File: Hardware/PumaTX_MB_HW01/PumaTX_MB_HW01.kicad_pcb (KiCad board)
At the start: 4 copper layers, 130 x 40 mm, 121 parts, among them J100 FH12A-26S-0.5SH_55_, J101 FH12-12S-0.5SH_55_, J102 500334-0160, J103 500334-0160, J104 692122030100, J105 53398-0667, J400 U.FL-R-SMT-1_40_, J410 U.FL-R-SMT-1_40_, M130 Motor_DC, M140 Fan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

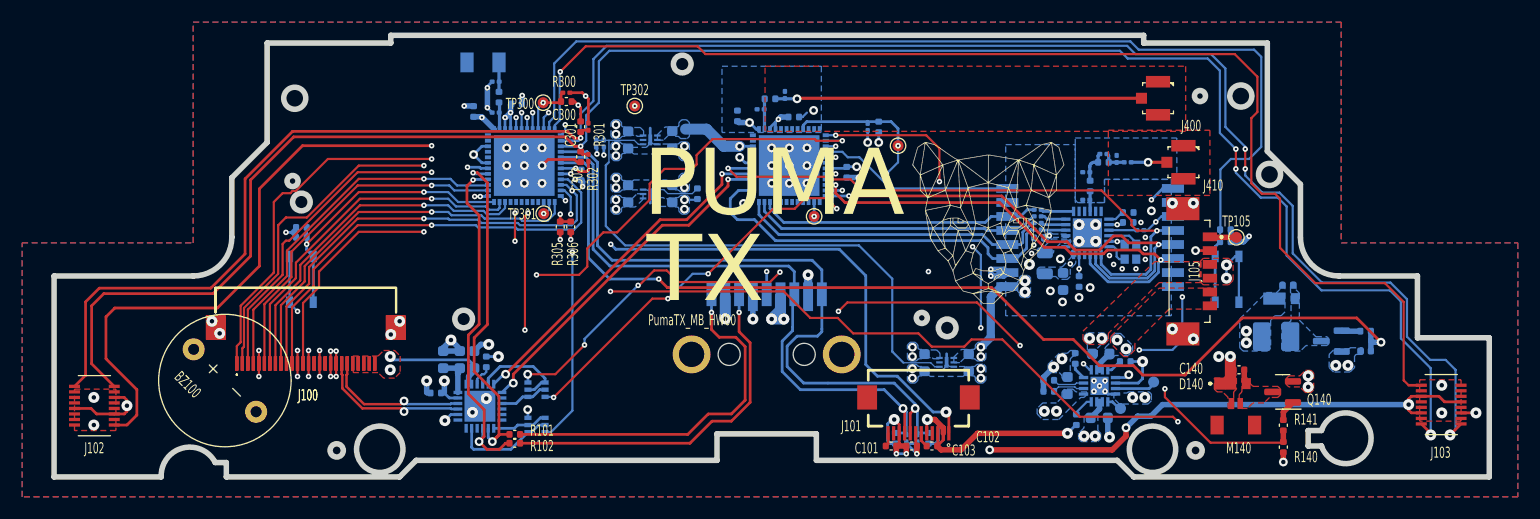
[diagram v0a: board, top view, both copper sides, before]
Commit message: MB_00 schematic done
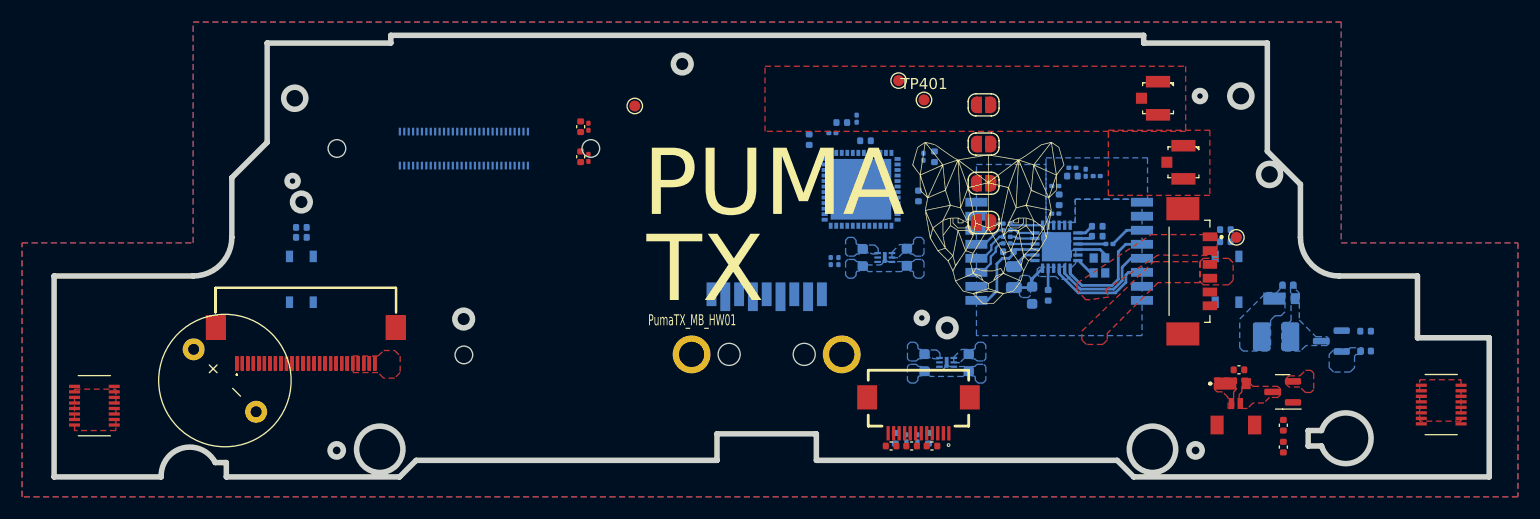
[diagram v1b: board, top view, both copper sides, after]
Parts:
- removed ANT300: 2450AT18A100E, Component_lib:ANTC3216X140N
- removed C200, C202, C501: 1u, Capacitor_SMD:C_0603_1608Metric
- removed C201: 100n, Capacitor_SMD:C_0603_1608Metric
- removed C203, C350: 100n, Capacitor_SMD:C_0402_1005Metric
- removed C300, C351: 1u, Capacitor_SMD:C_0402_1005Metric
- removed C306, C307: C, Capacitor_SMD:C_0201_0603Metric
- removed C352: 10u, Capacitor_SMD:C_0402_1005Metric
- removed C502, C503: 4u7, Capacitor_SMD:C_0603_1608Metric
- removed C510, C511: 2u2, Capacitor_SMD:C_0603_1608Metric
- removed L300: L, Capacitor_SMD:C_0402_1005Metric
- removed Q200, Q201: UMH3NTN, Component_lib:UMH3NTN
- removed R101, R102, R510: 0k, Capacitor_SMD:C_0402_1005Metric
- removed R200: 4k7, Capacitor_SMD:C_0402_1005Metric
- removed R300: 10k, Capacitor_SMD:C_0201_0603Metric
- removed R305: 120k, Capacitor_SMD:C_0402_1005Metric
- removed R306: 470k, Capacitor_SMD:C_0402_1005Metric
- removed R501: 100k, Capacitor_SMD:C_0402_1005Metric
- removed R502: 1k1, Capacitor_SMD:C_0402_1005Metric
- removed R503: 590, Capacitor_SMD:C_0402_1005Metric
- removed R504: 0, Capacitor_SMD:C_0402_1005Metric
- removed R505: 36k5, Capacitor_SMD:C_0402_1005Metric
- removed TP300: PUMATX_PU, TestPoint:TestPoint_Pad_D1.0mm
- removed TP301: VDD_SDIO, TestPoint:TestPoint_Pad_D1.0mm
- removed TP501: BQ_PGOOD, TestPoint:TestPoint_Pad_D1.0mm
- removed TP502: BQ_CHG, TestPoint:TestPoint_Pad_D1.0mm
- removed U200: CP2105-F01-GMR, Component_lib:QFN50P400X400X80-25N-D
- removed U300: ESP32-PICO-D4, Component_lib:ESP32-PICO-D4_1
- removed U500: BQ24075RGTR, Component_lib:QFN50P300X300X100-17N-D
- removed U510: MIC5528-3.3YMT-T5, Component_lib:SON40P120X120X60-7N-D
- added J1: PSoM_ESP32S2_Carrier_Board, Component_lib:PSoM_ESP32S2_00, B.Cu at (118.5, 93.5)
- added JP1: Jumper_2_Small_Open, Jumper:SolderJumper-2_P1.3mm_Open_RoundedPad1.0x1.5mm, F.Cu at (165.6, 89.5)
- added JP2: Jumper_2_Small_Open, Jumper:SolderJumper-2_P1.3mm_Open_RoundedPad1.0x1.5mm, F.Cu at (165.6, 93.0)
- added JP3: Jumper_2_Small_Open, Jumper:SolderJumper-2_P1.3mm_Open_RoundedPad1.0x1.5mm, F.Cu at (165.6, 96.6)
- added JP4: Jumper_2_Small_Open, Jumper:SolderJumper-2_P1.3mm_Open_RoundedPad1.0x1.5mm, F.Cu at (165.6, 100.2)
- moved C520 23.8 mm to (154.7, 103.3)
- moved R511 23.8 mm to (152.4, 103.7)
- moved R512 23.8 mm to (151.8, 103.7)
- moved U520 23.8 mm to (156.7, 103.3)
- moved C521 23.8 mm to (158.7, 103.3)
- moved TP401 14.5 mm to (160.2, 89.0)
- moved C407 6.85 mm to (154.1, 90.8)
- moved C450 6.85 mm to (149.8, 92.7)
- moved C451 6.85 mm to (159.7, 97.8)
- moved C452 6.85 mm to (154.9, 92.8)
- moved U400 6.85 mm to (154.5, 97.2)
- moved C406 6.85 mm to (151.9, 92.0)
- moved L400 6.85 mm to (152.8, 91.1)
- moved TP400 5.90 mm to (157.9, 87.3)
- moved C401 5.73 mm to (161.2, 94.2)
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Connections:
- J104 pad 2: VBUS -> Net-(J104-D-)
- J104 pad 3: +3V3 -> Net-(J104-D+)
- J105 pad 1: /BATTERY_WHITE -> /VBAT
- J105 pad 2: /BATTERY_TEMP -> /VBAT
- J105 pad 5: /VBAT -> /BATTERY_TEMP
- J105 pad 6: /VBAT -> /BATTERY_WHITE
- M140 pad 3: GND -> (no net)
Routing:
- net +3V3: track 293.3 -> 0.00 mm, vias 20 -> 0
- net /PUMATX_SDA: track 181.8 -> 0.00 mm, vias 4 -> 0
- net /PUMATX_SCL: track 178.9 -> 0.00 mm, vias 4 -> 0
- net /RIGHT_POT: track 110.3 -> 0.00 mm, vias 1 -> 0
- net /SPORT: track 109.2 -> 0.00 mm, vias 6 -> 0
- net /VSYS: track 106.6 -> 0.00 mm, vias 14 -> 0
- net VBUS: track 106.4 -> 0.00 mm, vias 6 -> 0
- net GND: track 106.1 -> 0.00 mm, vias 123 -> 0
- net /C2: track 96.5 -> 0.00 mm
- net /HAPTIC_PWM: track 92.9 -> 0.00 mm, vias 2 -> 0
- net /BUZZER_PWM: track 70.5 -> 0.00 mm, vias 2 -> 0
- net /FAN_PWM: track 62.8 -> 0.00 mm, vias 5 -> 0
- net /DISPLAY_SCL: track 62.8 -> 0.00 mm, vias 1 -> 0
- net /LEFT_POT: track 62.3 -> 0.00 mm, vias 2 -> 0
- net /ELRS_CHIP_PU: track 59.1 -> 0.00 mm, vias 6 -> 0
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- removed copper zone on B.Cu, net +3V3
- removed copper zone on B.Cu, net /VBAT
- removed copper zone on B.Cu, net VBUS
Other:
- board text added: "PumaTX_MB_HW01"
- board text removed: "PumaTX_MB_HW00"

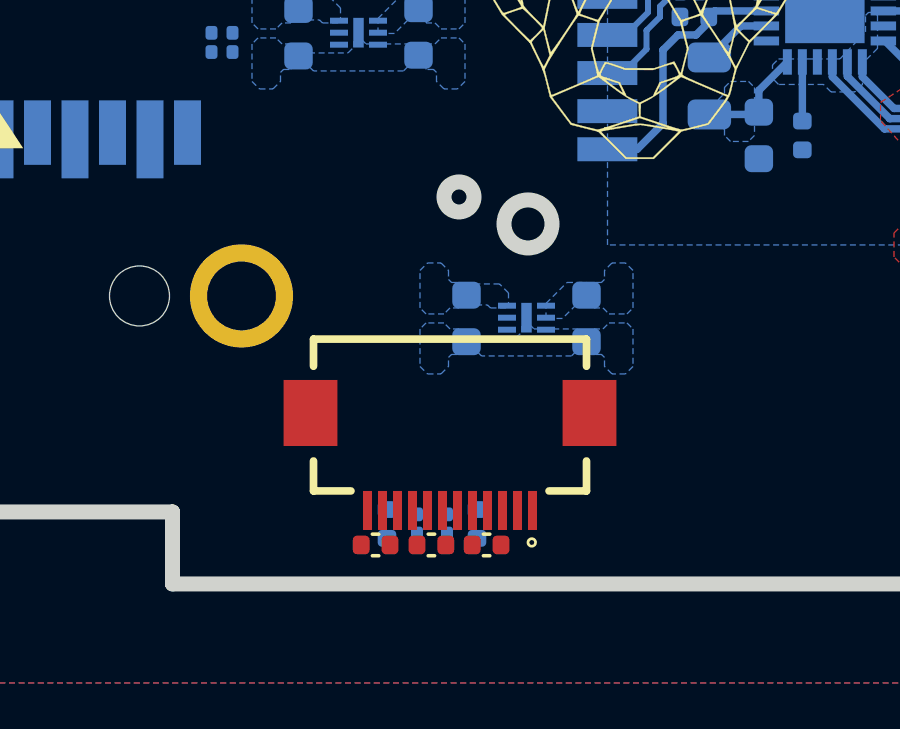
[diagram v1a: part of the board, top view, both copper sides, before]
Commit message: updated display connector
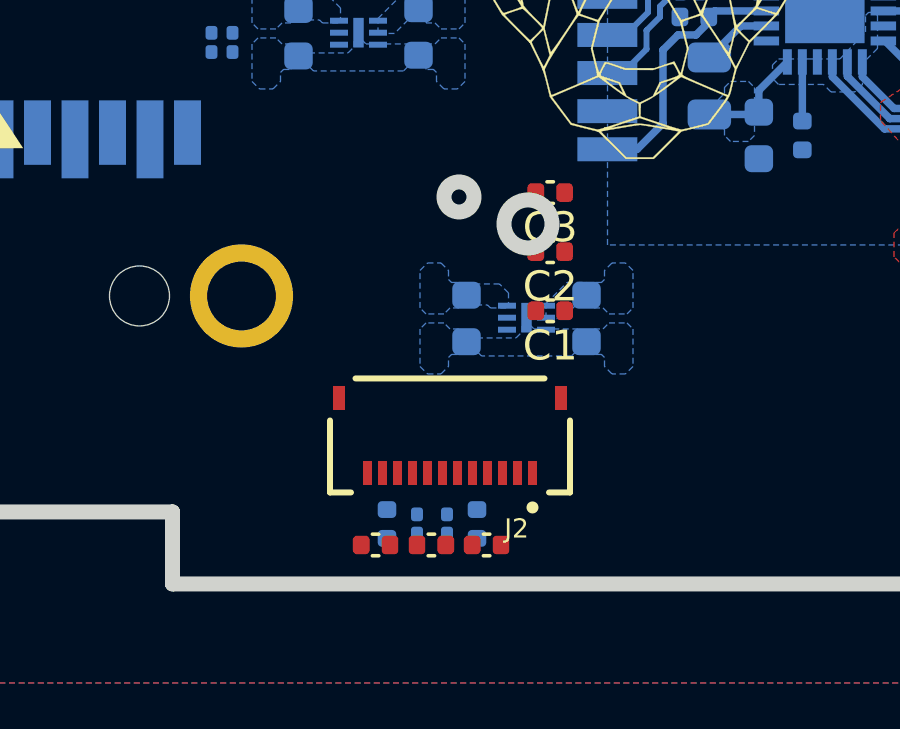
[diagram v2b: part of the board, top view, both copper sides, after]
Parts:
- removed J101: FH12-12S-0.5SH_55_, Component_lib:FH12-12S-0.5SH_55_
- added C1: 2n2, Capacitor_SMD:C_0402_1005Metric, F.Cu at (163.0, 112.6)
- added C2: 1n, Capacitor_SMD:C_0402_1005Metric, F.Cu at (163.0, 110.6)
- added C3: 15u, Capacitor_SMD:C_0402_1005Metric, F.Cu at (163.0, 108.7)
- added J2: FFC2B28-12-G, Component_lib:GCT_FFC2B28-12-G, F.Cu at (159.7, 116.8)
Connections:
- J1 pad 11: unconnected-(J1-IO5-Pad11) -> /PHOTO
- J1 pad 23: unconnected-(J1-IO11-Pad23) -> /SPORT
- J1 pad 25: unconnected-(J1-IO12-Pad25) -> /C1
- J1 pad 27: unconnected-(J1-IO13-Pad27) -> /C2
- J1 pad 29: unconnected-(J1-IO14-Pad29) -> /UP
- J1 pad 31: unconnected-(J1-IO15-Pad31) -> /DOWN
- J1 pad 33: unconnected-(J1-IO16-Pad33) -> /RIGHT
- J1 pad 35: unconnected-(J1-IO17/DAC-Pad35) -> /LEFT
- J1 pad 37: unconnected-(J1-IO18/DAC-Pad37) -> /OK
- J1 pad 38: unconnected-(J1-IO37-Pad38) -> /ELRS_GPIO0
- J1 pad 40: unconnected-(J1-IO38-Pad40) -> /ELRS_CHIP_PU
- J1 pad 5: unconnected-(J1-IO2-Pad5) -> /RTH
- J1 pad 7: unconnected-(J1-IO3-Pad7) -> /PAUSE
- J1 pad 9: unconnected-(J1-IO4-Pad9) -> /RECORD
- J100 pad 15: unconnected-(J100-Pad15) -> +3V3 (x2)
